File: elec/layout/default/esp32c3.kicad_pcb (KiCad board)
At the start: 2 copper layers, 7 parts

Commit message: Update esp32c3.kicad_pcb
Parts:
- removed R4: Chip Resistor - Surface Mount 10KOhms ±5% 1/10W 0603 RoHS, lib:R0603
- added R3: Chip Resistor - Surface Mount 10KOhms ±5% 1/10W 0603 RoHS, lib:R0603, F.Cu at (156.4, 105.2)
- C1: value Multilayer Ceramic Capacitors MLCC - SMD/SMT 10uF 16V 0603 RoHS -> Multilayer Ceramic Capacitors MLCC - SMD/SMT 1uF 50V 0603 RoHS
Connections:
- U1 pad 10: nc -> (no net)
- U1 pad 15: nc -> (no net)
- U1 pad 17: nc -> (no net)
- U1 pad 24: nc -> (no net)
- U1 pad 25: nc -> (no net)
- U1 pad 28: nc -> (no net)
- U1 pad 29: nc -> (no net)
- U1 pad 32: nc -> (no net)
- U1 pad 33: nc -> (no net)
- U1 pad 34: nc -> (no net)
- U1 pad 35: nc -> (no net)
- U1 pad 4: nc -> (no net)
- U1 pad 7: nc -> (no net)
- U1 pad 9: nc -> (no net)
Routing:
- net gnd: track 45.9 -> 1.13 mm
- net en: track 4.31 -> 4.85 mm

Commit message: added signals to GPIO
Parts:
- C1: value Multilayer Ceramic Capacitors MLCC - SMD/SMT 1uF 50V 0603 RoHS -> 50V 1uF X5R ±10% 0603 Multilayer Ceramic Capacitors MLCC - SMD/SMT ROHS
- C2: value Multilayer Ceramic Capacitors MLCC - SMD/SMT 10uF 16V 0603 RoHS -> 10V 10uF X5R ±10% 0603 Multilayer Ceramic Capacitors MLCC - SMD/SMT ROHS
- C3: value Multilayer Ceramic Capacitors MLCC - SMD/SMT 100nF 50V 0603 RoHS -> 50V 100nF X7R ±10% 0603 Multilayer Ceramic Capacitors MLCC - SMD/SMT ROHS
- R1, R2, R3: value Chip Resistor - Surface Mount 10KOhms ±5% 1/10W 0603 RoHS -> 100mW Thick Film Resistors ±100ppm/℃ ±1% 10kΩ 0603 Chip Resistor - Surface Mount ROHS
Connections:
- net io18 renamed dm
- net io19 renamed dp
- net rxd0 renamed rx
- net txd0 renamed tx
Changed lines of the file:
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@@
   (net 13 "io8")
   (net 14 "io9")
-  (net 15 "io18")
-  (net 16 "io19")
-  (net 17 "rxd0")
-  (net 18 "txd0")
+  (net 15 "dm")
+  (net 16 "dp")
+  (net 17 "rx")
+  (net 18 "tx")
   (footprint "lib:R0603" (layer "F.Cu")
     (at 156.4 108.4)
@@
         (effects (font (size 1 1) (thickness 0.15)))
     )
-    (fp_text value "Chip Resistor - Surface Mount 10KOhms ±5% 1/10W 0603 RoHS" (at 0 1.43) (layer "F.Fab") hide
+    (fp_text value "100mW Thick Film Resistors ±100ppm/℃ ±1% 10kΩ 0603  Chip Resistor - Surface Mount ROHS" (at 0 1.43) (layer "F.Fab") hide
         (effects (font (size 1 1) (thickness 0.15)))
     )
@@
         (effects (font (size 1 1) (thickness 0.15)))
     )
-    (fp_text value "Chip Resistor - Surface Mount 10KOhms ±5% 1/10W 0603 RoHS" (at 0 1.43) (layer "F.Fab") hide
+    (fp_text value "100mW Thick Film Resistors ±100ppm/℃ ±1% 10kΩ 0603  Chip Resistor - Surface Mount ROHS" (at 0 1.43) (layer "F.Fab") hide
         (effects (font (size 1 1) (thickness 0.15)))
     )
@@
         (effects (font (size 1 1) (thickness 0.15)))
     )
-    (fp_text value "Chip Resistor - Surface Mount 10KOhms ±5% 1/10W 0603 RoHS" (at 0 1.43) (layer "F.Fab") hide
+    (fp_text value "100mW Thick Film Resistors ±100ppm/℃ ±1% 10kΩ 0603  Chip Resistor - Surface Mount ROHS" (at 0 1.43) (layer "F.Fab") hide
         (effects (font (size 1 1) (thickness 0.15)))
     )
@@
         (effects (font (size 1 1) (thickness 0.15)))
     )
-    (fp_text value "Multilayer Ceramic Capacitors MLCC - SMD/SMT 10uF 16V 0603 RoHS" (at 0 1.43) (layer "F.Fab") hide
+    (fp_text value "10V 10uF X5R ±10% 0603  Multilayer Ceramic Capacitors MLCC - SMD/SMT ROHS" (at 0 1.43) (layer "F.Fab") hide
         (effects (font (size 1 1) (thickness 0.15)))
     )
@@
     (fp_circle (center -7.2 -4.21) (end -7 -4.21)
       (stroke (width 0.25) (type solid)) (fill none) (layer "F.SilkS"))
-    (fp_circle (center -6.4 -4) (end -6.2 -4)
-      (stroke (width 0.4) (type solid)) (fill none) (layer "Cmts.User"))
     (fp_circle (center -6.6 -6.9) (end -6.57 -6.9)
       (stroke (width 0.06) (type solid)) (fill none) (layer "F.Fab"))
@@
     (pad "25" smd rect (at 5.9 4) (size 1 0.5) (layers "F.Cu" "F.Paste" "F.Mask"))
     (pad "26" smd rect (at 5.9 3.2) (size 1 0.5) (layers "F.Cu" "F.Paste" "F.Mask")
-      (net 15 "io18") (pintype "stereo"))
+      (net 15 "dm") (pintype "stereo"))
     (pad "27" smd rect (at 5.9 2.4) (size 1 0.5) (layers "F.Cu" "F.Paste" "F.Mask")
-      (net 16 "io19") (pintype "stereo"))
+      (net 16 "dp") (pintype "stereo"))
     (pad "28" smd rect (at 5.9 1.6) (size 1 0.5) (layers "F.Cu" "F.Paste" "F.Mask"))
     (pad "29" smd rect (at 5.9 0.8) (size 1 0.5) (layers "F.Cu" "F.Paste" "F.Mask"))
     (pad "30" smd rect (at 5.9 0) (size 1 0.5) (layers "F.Cu" "F.Paste" "F.Mask")
-      (net 17 "rxd0") (pintype "stereo"))
+      (net 17 "rx") (pintype "stereo"))
     (pad "31" smd rect (at 5.9 -0.8) (size 1 0.5) (layers "F.Cu" "F.Paste" "F.Mask")
-      (net 18 "txd0") (pintype "stereo"))
+      (net 18 "tx") (pintype "stereo"))
     (pad "32" smd rect (at 5.9 -1.6) (size 1 0.5) (layers "F.Cu" "F.Paste" "F.Mask"))
     (pad "33" smd rect (at 5.9 -2.4) (size 1 0.5) (layers "F.Cu" "F.Paste" "F.Mask"))
@@
         (effects (font (size 1 1) (thickness 0.15)))
     )
-    (fp_text value "Multilayer Ceramic Capacitors MLCC - SMD/SMT 100nF 50V 0603 RoHS" (at 0 1.43) (layer "F.Fab") hide
+    (fp_text value "50V 100nF X7R ±10% 0603  Multilayer Ceramic Capacitors MLCC - SMD/SMT ROHS" (at 0 1.43) (layer "F.Fab") hide
         (effects (font (size 1 1) (thickness 0.15)))
     )
@@
         (effects (font (size 1 1) (thickness 0.15)))
     )
-    (fp_text value "Multilayer Ceramic Capacitors MLCC - SMD/SMT 1uF 50V 0603 RoHS" (at 0 1.43) (layer "F.Fab") hide
-        (effects (font (size 1 1) (thickness 0.15)))
-    )
+    (fp_text value "50V 1uF X5R ±10% 0603  Multilayer Ceramic Capacitors MLCC - SMD/SMT ROHS" (at 0 1.43) (layer "F.Fab") hide
+        (effects (font (size 1 1) (thickness 0.15)))
+    )

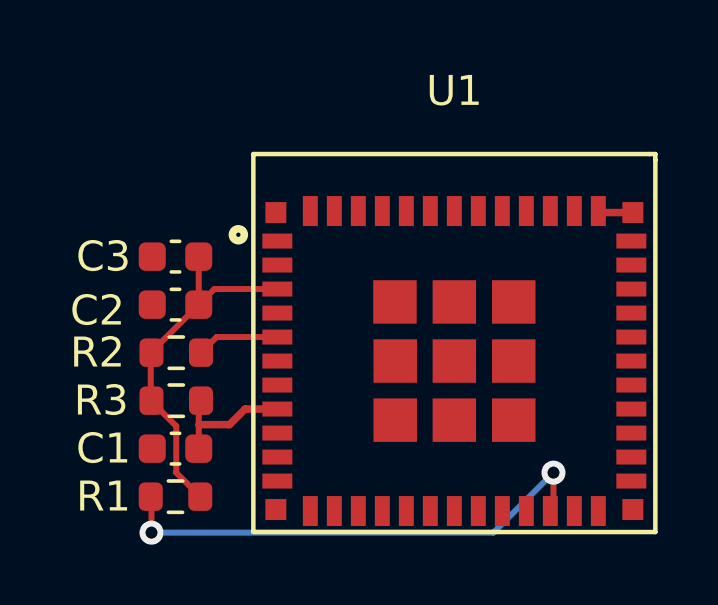
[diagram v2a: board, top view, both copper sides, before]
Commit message: Both variants added
External antenna and PCB antenna variants usable from this package.
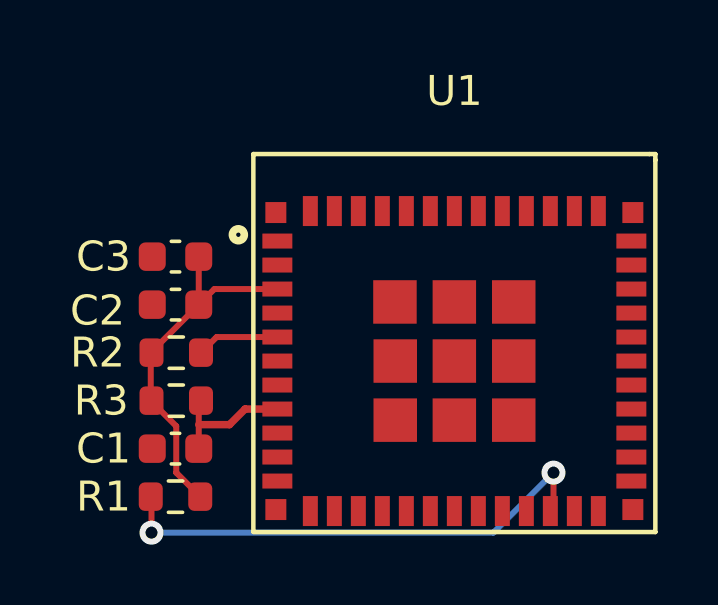
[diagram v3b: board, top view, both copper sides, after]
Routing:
- net gnd: track 1.13 -> 0.14 mm
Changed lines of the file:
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@@
   )
   (segment (start 159.745 107.93) (end 159.795 107.88) (width 0.25) (layer "F.Cu") (net 1))
-  (segment (start 170.655 98.93) (end 171.645 98.93) (width 0.25) (layer "F.Cu") (net 1))
   (segment (start 159.745 100.63) (end 159.795 100.68) (width 0.25) (layer "F.Cu") (net 1))
   (segment (start 155.6 103.575) (end 157.175 102) (width 0.2) (layer "F.Cu") (net 2))
